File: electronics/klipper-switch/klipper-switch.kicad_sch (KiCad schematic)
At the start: 0 parts

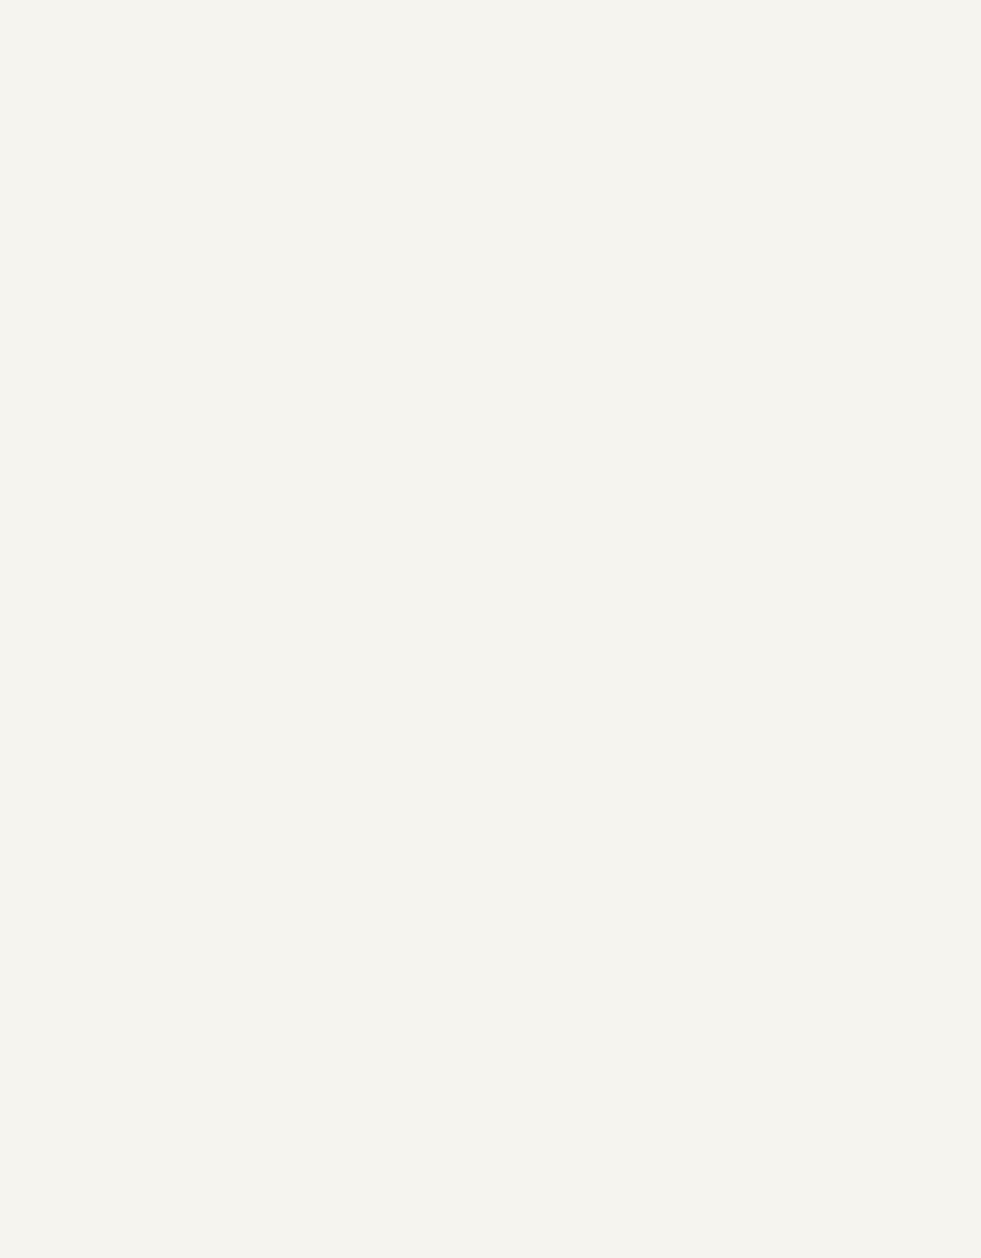
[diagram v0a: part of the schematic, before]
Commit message: created schematic pages
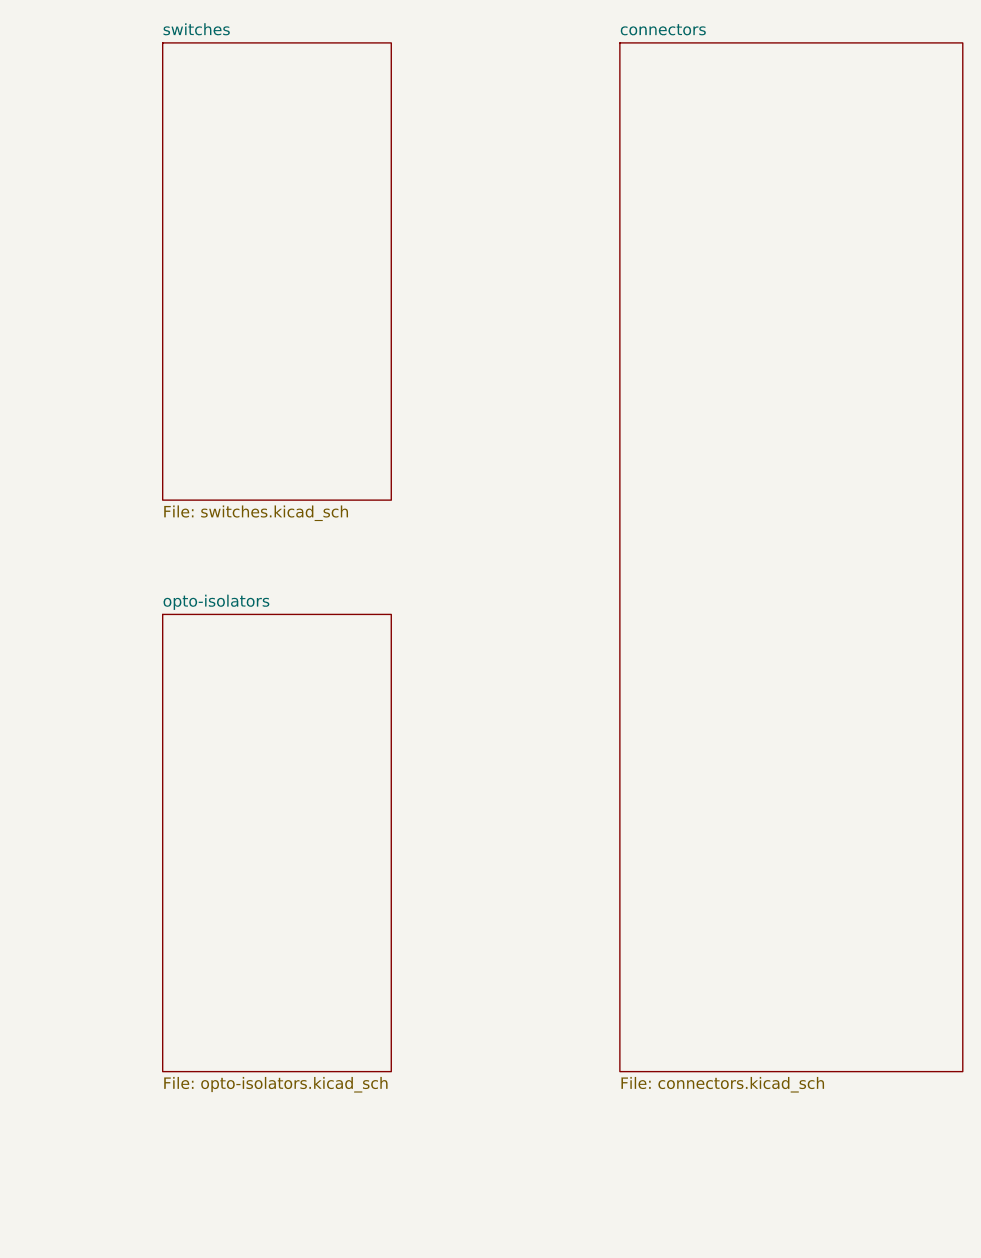
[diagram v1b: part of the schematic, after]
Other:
- added sheet connectors (connectors.kicad_sch)
- added sheet opto-isolators (opto-isolators.kicad_sch)
- added sheet switches (switches.kicad_sch)
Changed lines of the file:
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@@
+		)
+	)
+	(sheet
+		(at 127 25.4)
+		(size 38.1 114.3)
+		(fields_autoplaced yes)
+		(stroke
+			(width 0.1524)
+			(type solid)
+		)
+		(fill
+			(color 0 0 0 0.0000)
+		)
+		(property "Sheetname" "connectors"
+			(at 127 24.6884 0)
+			(effects
+				(font
+					(size 1.27 1.27)
+				)
+				(justify left bottom)
+			)
+		)
+		(property "Sheetfile" "connectors.kicad_sch"
+			(at 127 140.2846 0)
+			(effects
+				(font
+					(size 1.27 1.27)
+				)
+				(justify left top)
+			)
+		)
+		(instances
+			(project "klipper-switch"
+				(path "/e5df92b1-e048-41e8-96e5-ed9a12dbef0e"
+					(page "5")
+				)
+			)
+		)
+	)
+	(sheet
+		(at 76.2 88.9)
+		(size 25.4 50.8)
+		(fields_autoplaced yes)
+		(stroke
+			(width 0.1524)
+			(type solid)
+		)
+		(fill
+			(color 0 0 0 0.0000)
+		)
+		(property "Sheetname" "opto-isolators"
+			(at 76.2 88.1884 0)
+			(effects
+				(font
+					(size 1.27 1.27)
+				)
+				(justify left bottom)
+			)
+		)
+		(property "Sheetfile" "opto-isolators.kicad_sch"
+			(at 76.2 140.2846 0)
+			(effects
+				(font
+					(size 1.27 1.27)
+				)
+				(justify left top)
+			)
+		)
+		(instances
+			(project "klipper-switch"
+				(path "/e5df92b1-e048-41e8-96e5-ed9a12dbef0e"
+					(page "4")
+				)
+			)
+		)
+	)
+	(sheet
+		(at 76.2 25.4)
+		(size 25.4 50.8)
+		(fields_autoplaced yes)
+		(stroke
+			(width 0.1524)
+			(type solid)
+		)
+		(fill
+			(color 0 0 0 0.0000)
+		)
+		(property "Sheetname" "switches"
+			(at 76.2 24.6884 0)
+			(effects
+				(font
+					(size 1.27 1.27)
+				)
+				(justify left bottom)
+			)
+		)
+		(property "Sheetfile" "switches.kicad_sch"
+			(at 76.2 76.7846 0)
+			(effects
+				(font
+					(size 1.27 1.27)
+				)
+				(justify left top)
+			)
+		)
+		(instances
+			(project "klipper-switch"
+				(path "/e5df92b1-e048-41e8-96e5-ed9a12dbef0e"
+					(page "3")
+				)
+			)
 		)
 	)

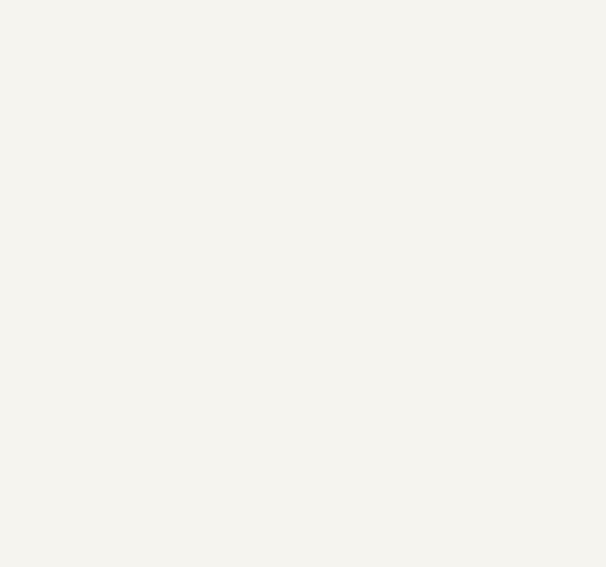
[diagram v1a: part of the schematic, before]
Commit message: Added BV1 Footprint properly and fixed my libraries
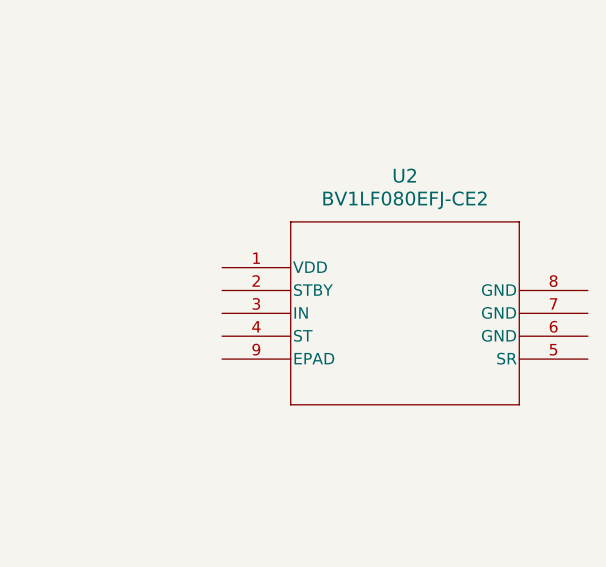
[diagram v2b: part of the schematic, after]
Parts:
- added U2: BV1LF080EFJ-CE2, BV1LF080EFJ-CE2_ROM, symbol klipper-switch:BV1LF080EFJ-CE2
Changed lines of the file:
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@@
 		(rev "V 1.0")
+	)
+	(symbol
+		(lib_id "klipper-switch:BV1LF080EFJ-CE2")
+		(at 226.06 63.5 0)
+		(unit 1)
+		(exclude_from_sim no)
+		(in_bom yes)
+		(on_board yes)
+		(dnp no)
+		(fields_autoplaced yes)
+		(property "Reference" "U2"
+			(at 246.38 53.34 0)
+			(effects
+				(font
+					(size 1.524 1.524)
+				)
+			)
+		)
+		(property "Value" "BV1LF080EFJ-CE2"
+			(at 246.38 55.88 0)
+			(effects
+				(font
+					(size 1.524 1.524)
+				)
+			)
+		)
+		(property "Footprint" "BV1LF080EFJ-CE2_ROM"
+			(at 246.38 80.01 0)
+			(effects
+				(font
+					(size 1.27 1.27)
+					(italic yes)
+				)
+				(hide yes)
+			)
+		)
+		(property "Datasheet" "BV1LF080EFJ-CE2"
+			(at 246.634 82.296 0)
+			(effects
+				(font
+					(size 1.27 1.27)
+					(italic yes)
+				)
+				(hide yes)
+			)
+		)
+		(property "Description" "Power Switch/Driver 1:1 N-Channel 7.5A 8-HTSOP-J"
+			(at 226.06 63.5 0)
+			(effects
+				(font
+					(size 1.27 1.27)
+				)
+				(hide yes)
+			)
+		)
+		(property "Manufacturer" "Rohm Semiconductor"
+			(at 226.06 63.5 0)
+			(effects
+				(font
+					(size 1.27 1.27)
+				)
+				(hide yes)
+			)
+		)
+		(property "Manufacturer#" "BV1LF080EFJ-CE2"
+			(at 226.06 63.5 0)
+			(effects
+				(font
+					(size 1.27 1.27)
+				)
+				(hide yes)
+			)
+		)
+		(property "Supplier" "Digikey"
+			(at 226.06 63.5 0)
+			(effects
+				(font
+					(size 1.27 1.27)
+				)
+				(hide yes)
+			)
+		)
+		(property "Supplier#" "846-BV1LF080EFJ-CE2CT-ND"
+			(at 226.06 63.5 0)
+			(effects
+				(font
+					(size 1.27 1.27)
+				)
+				(hide yes)
+			)
+		)
+		(property "Role" ""
+			(at 226.06 63.5 0)
+			(effects
+				(font
+					(size 1.27 1.27)
+				)
+				(hide yes)
+			)
+		)
+		(pin "5"
+		)
+		(pin "7"
+		)
+		(pin "9"
+		)
+		(pin "2"
+		)
+		(pin "3"
+		)
+		(pin "6"
+		)
+		(pin "1"
+		)
+		(pin "8"
+		)
+		(pin "4"
+		)
+		(instances
+			(project ""
+				(path "/e5df92b1-e048-41e8-96e5-ed9a12dbef0e"
+					(reference "U2")
+					(unit 1)
+				)
+			)
+		)
 	)
 	(sheet
